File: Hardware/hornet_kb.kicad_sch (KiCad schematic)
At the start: 34 parts, among them J1 Conn_ST_STDC14, J10 USB_C_Receptacle_USB2.0, SW98 SW_Push, U1 nRF52840, Y1 32.768kHz, Y3 Crystal_GND24

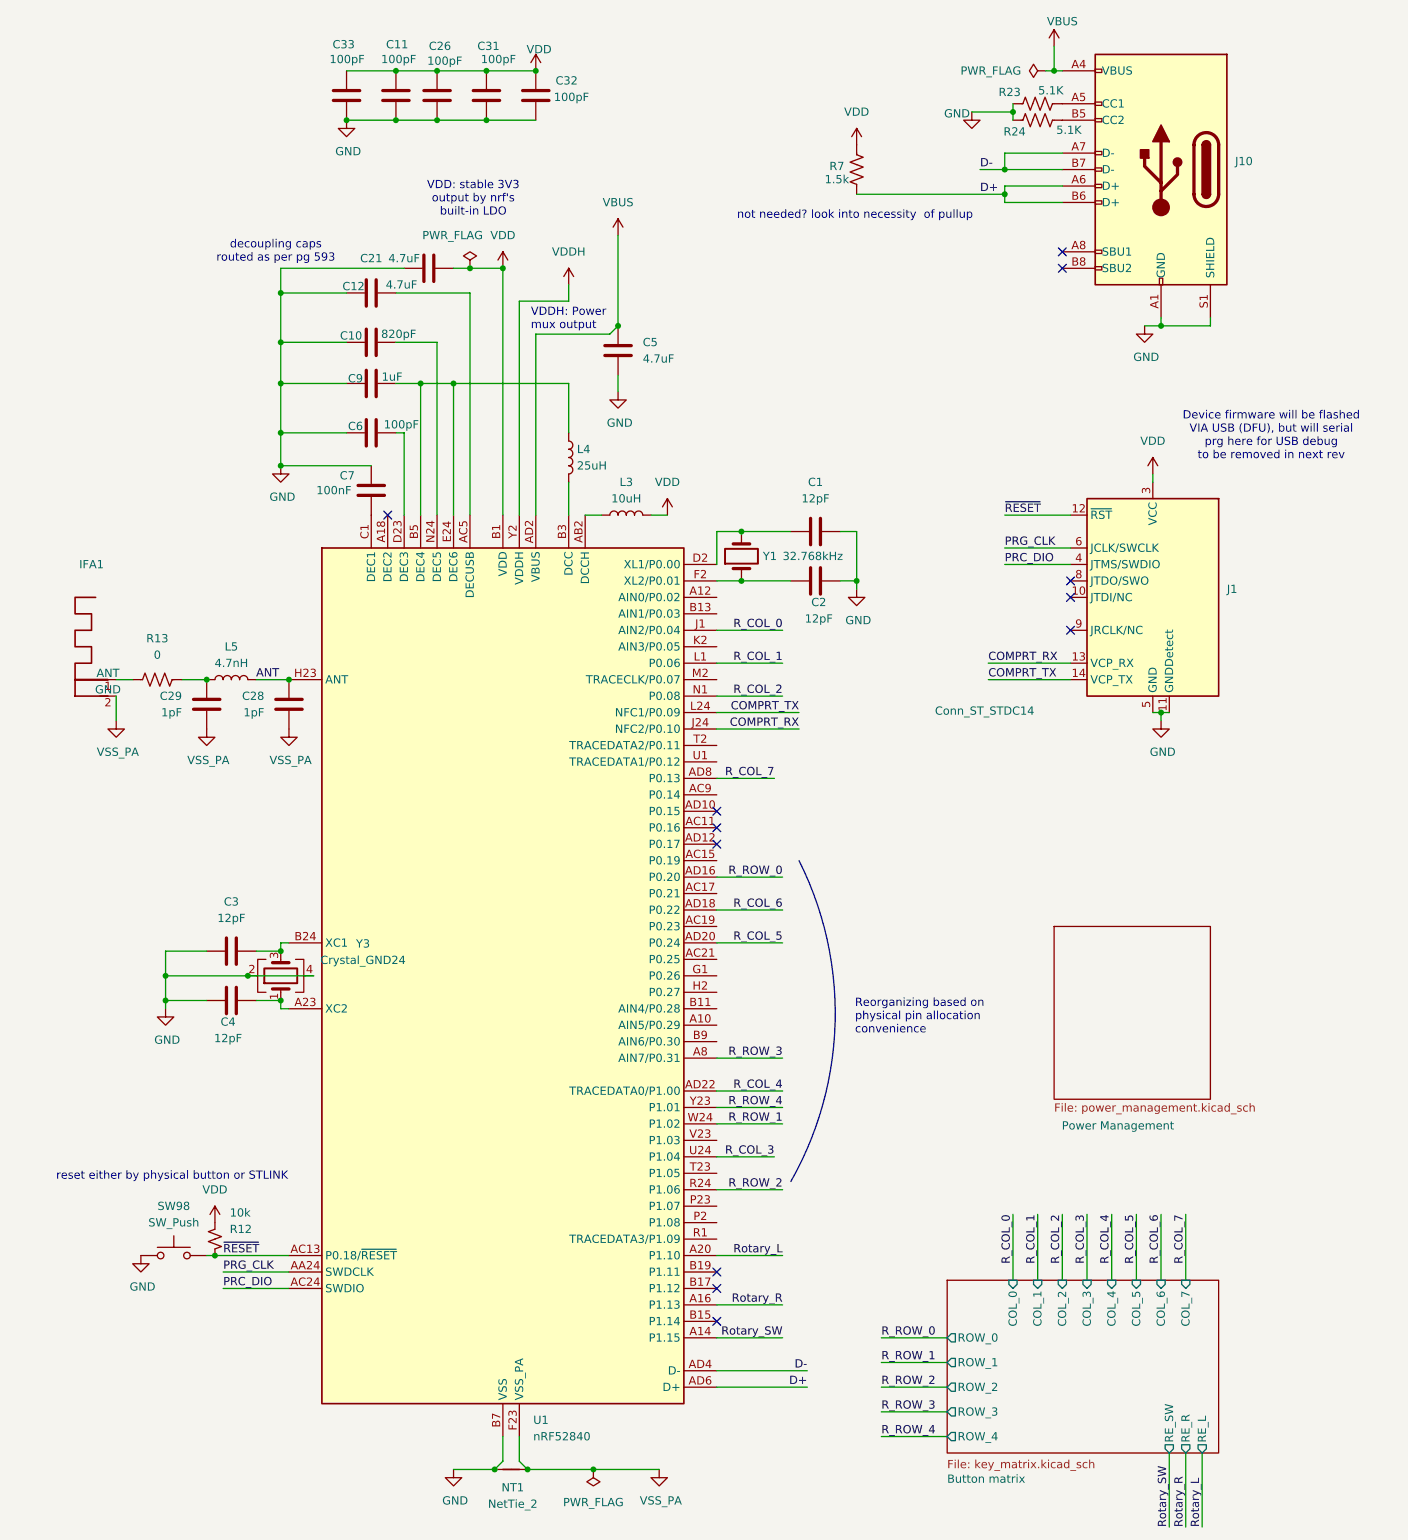
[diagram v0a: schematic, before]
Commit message: Resolving DRC errors
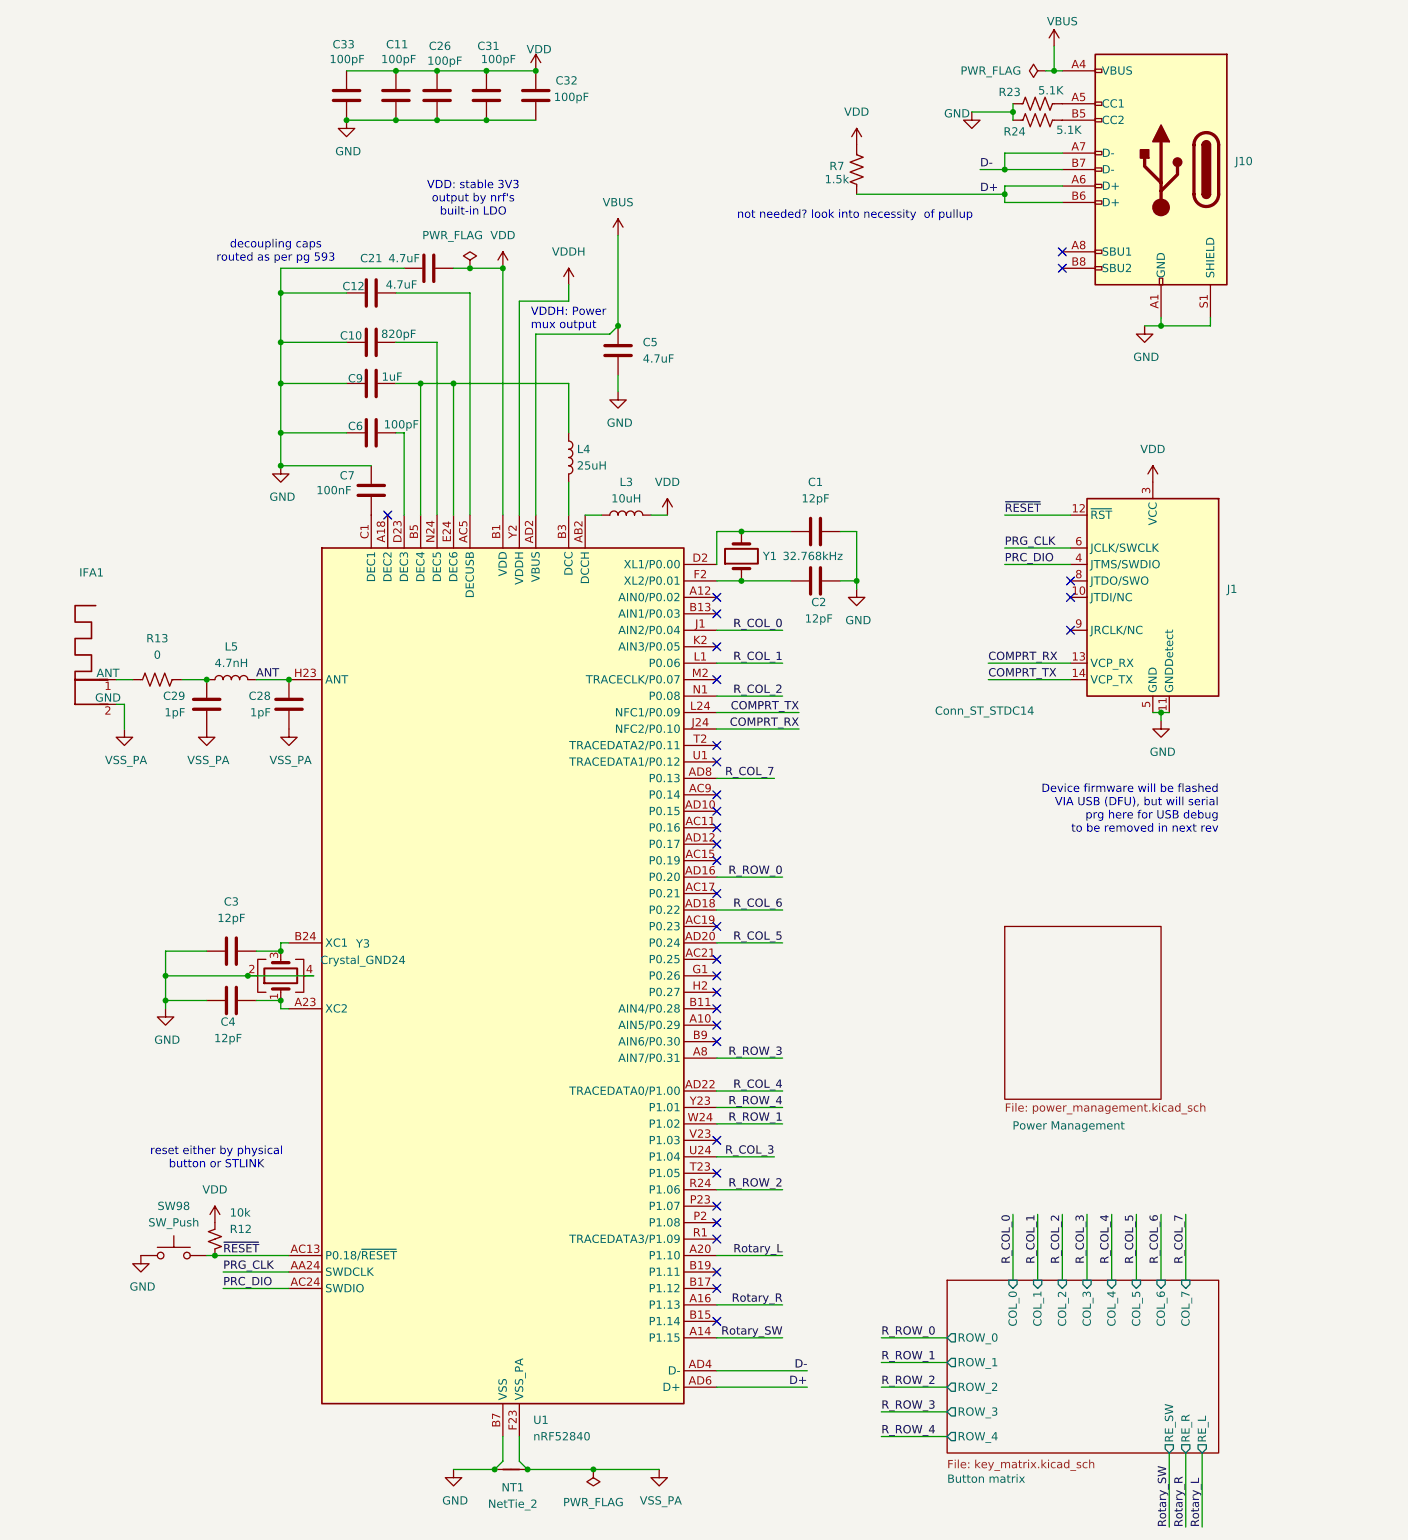
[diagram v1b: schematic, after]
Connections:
- no-connect marks 12 -> 33
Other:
- note removed: "Reorganizing based on physical pin allocation convenience"
- moved on the sheet: IFA1

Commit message: Change reset switchto custom footprint
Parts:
- SW98: footprint Button_Switch_SMD:SW_Push_1P1T-MP_NO_Horizontal_Alps_SKRTLAE010 -> ScottoKeebs_Miscellaneous:SW_DIP_SPSTx01_Slide_6.7x4.1mm_W6.73mm_P2.54mm_LowProfile_JPin
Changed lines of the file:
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@@
 			)
 		)
-		(property "Footprint" "Button_Switch_SMD:SW_Push_1P1T-MP_NO_Horizontal_Alps_SKRTLAE010"
+		(property "Footprint" "ScottoKeebs_Miscellaneous:SW_DIP_SPSTx01_Slide_6.7x4.1mm_W6.73mm_P2.54mm_LowProfile_JPin"
 			(at 29.21 200.66 0)
 			(effects

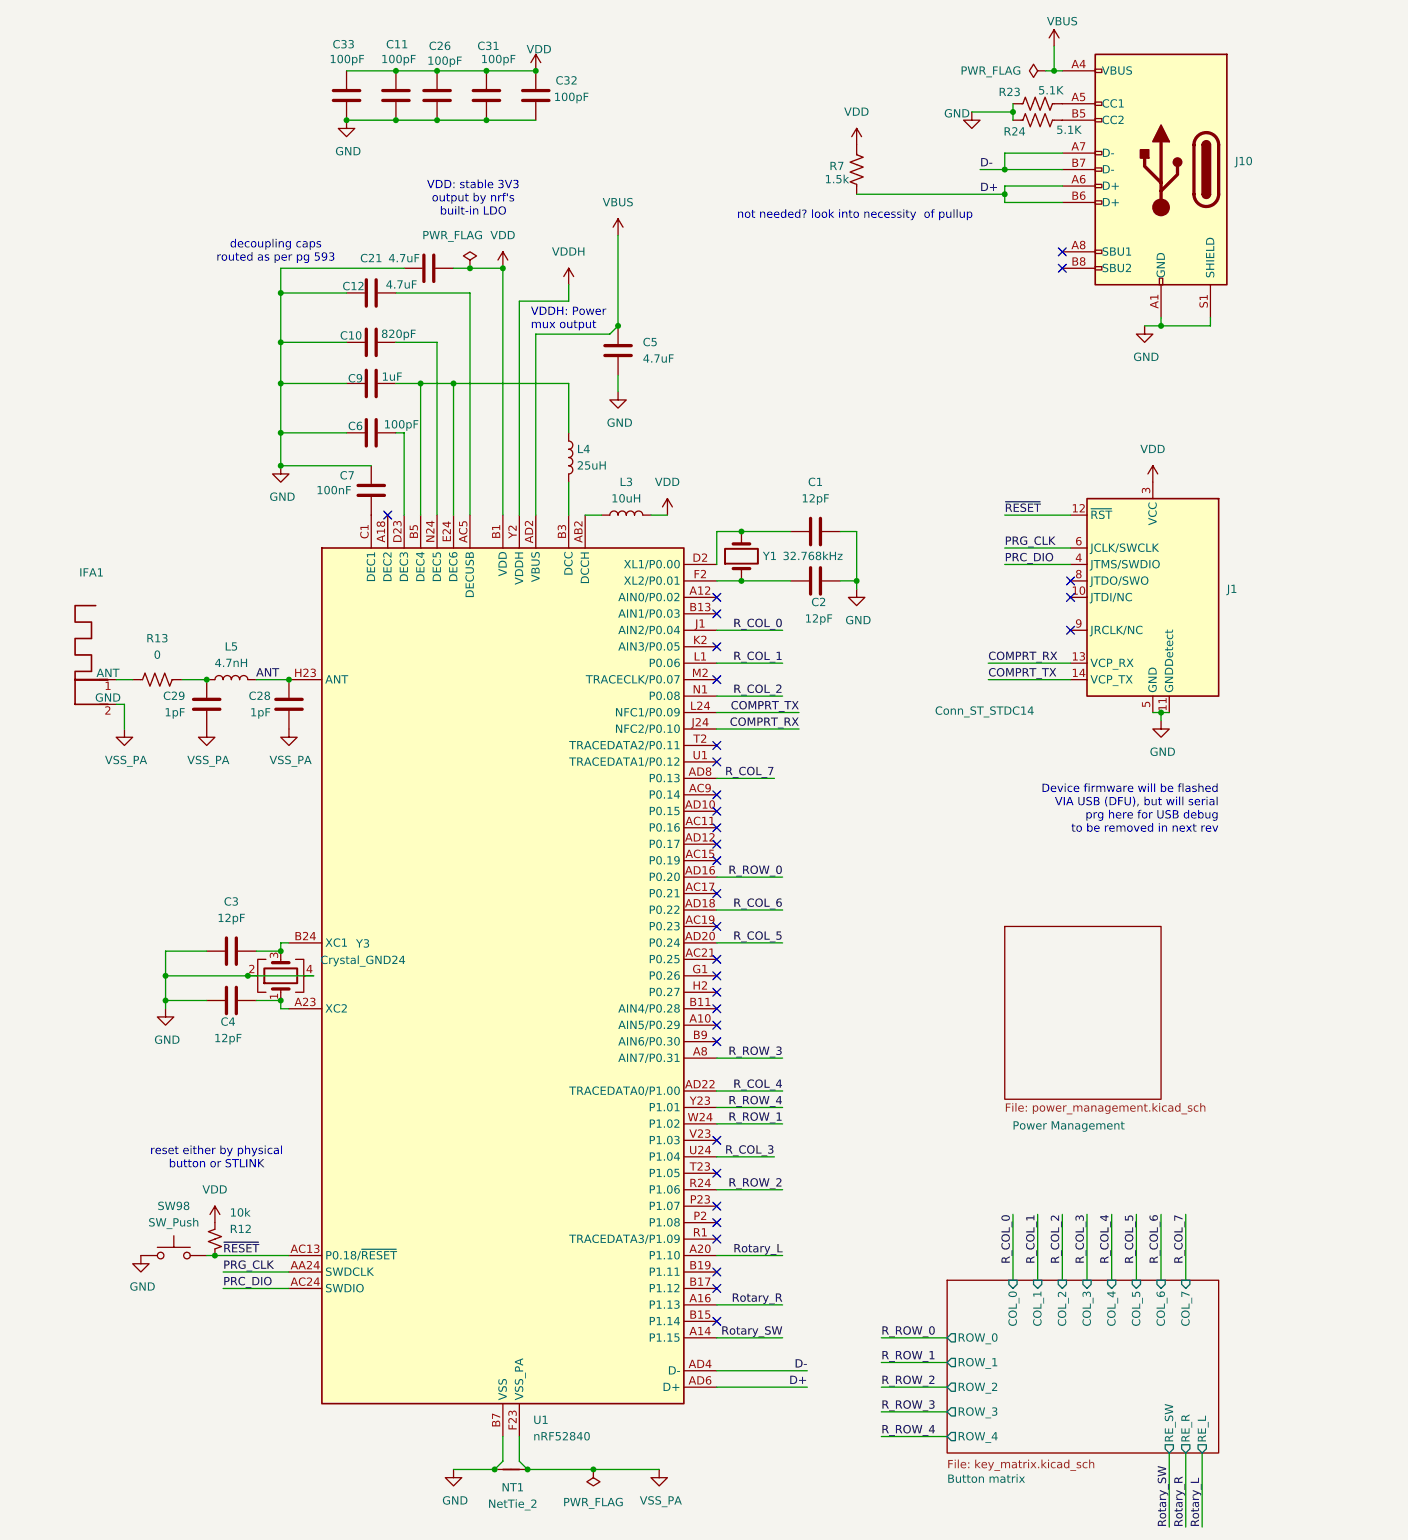
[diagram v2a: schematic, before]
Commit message: added mounting holes
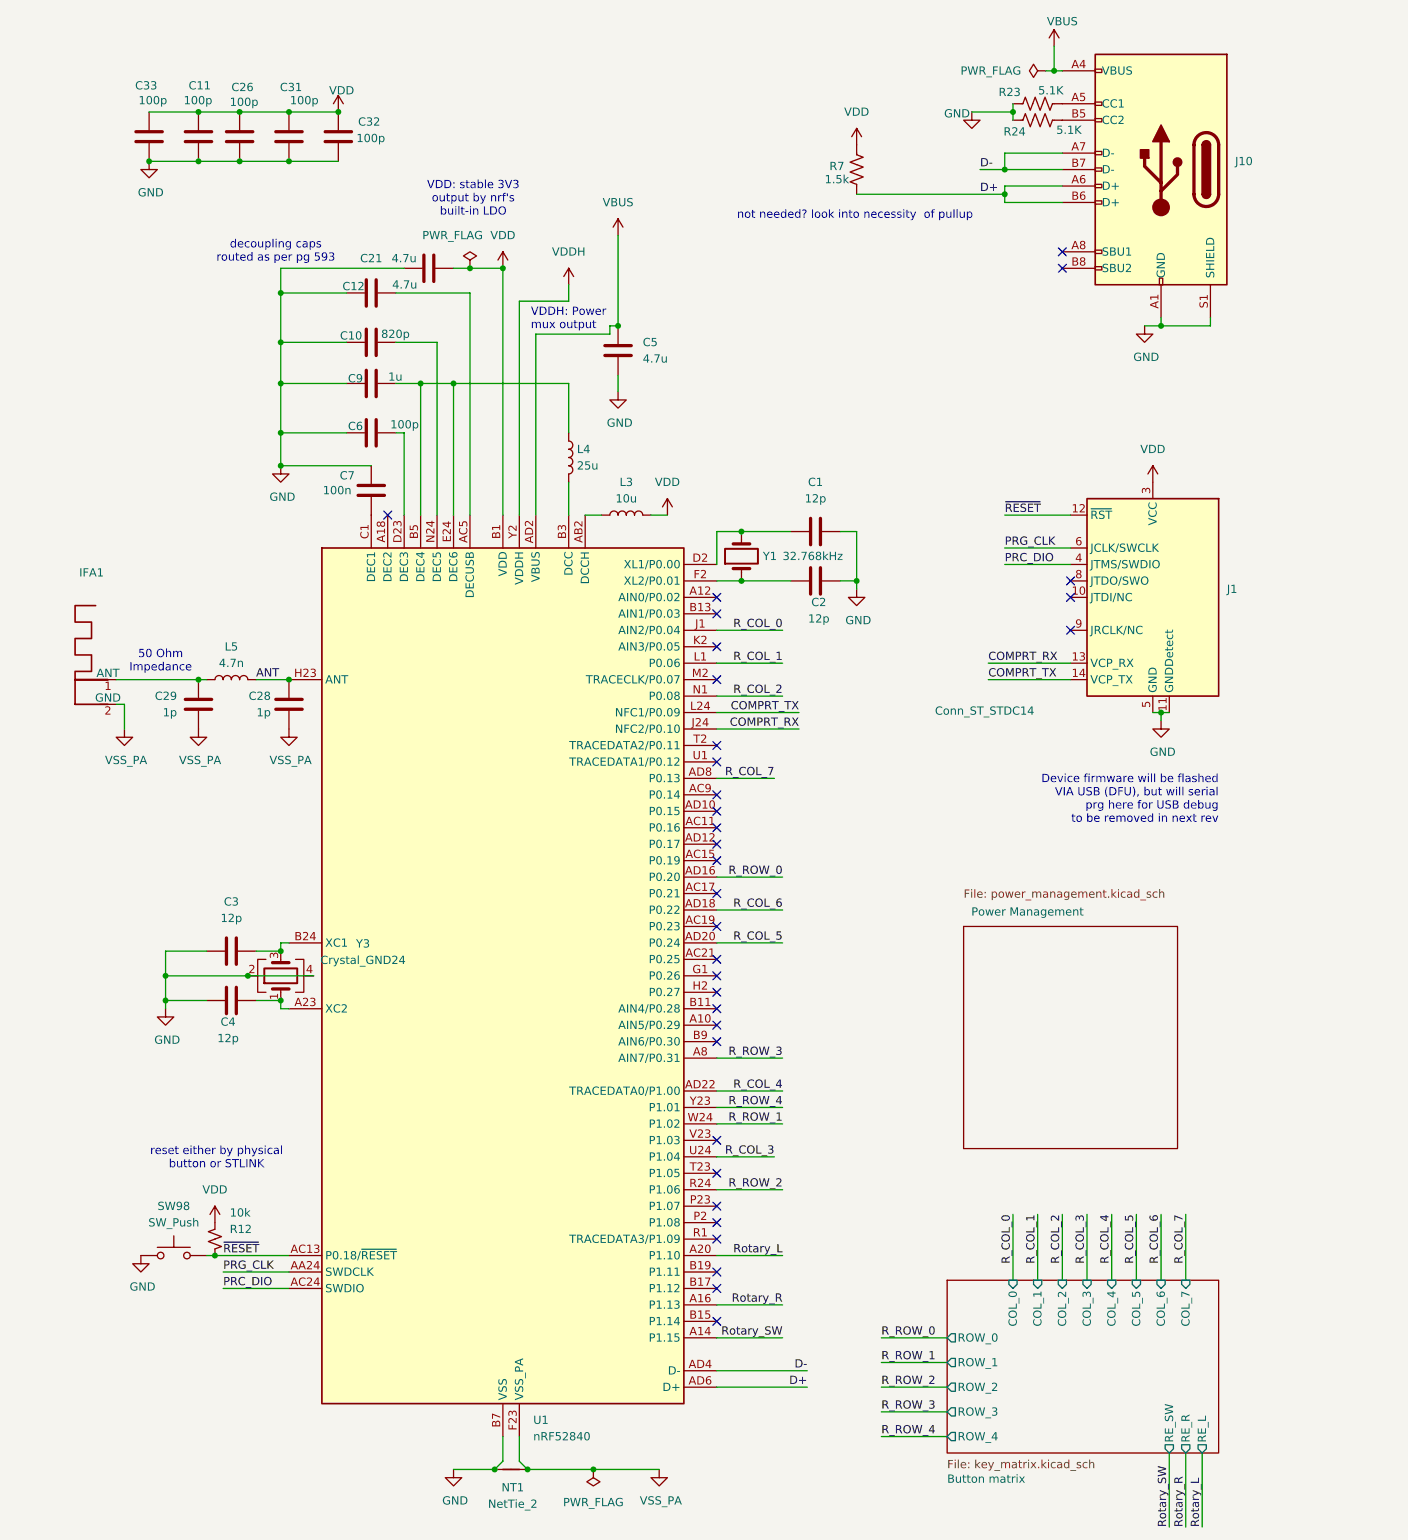
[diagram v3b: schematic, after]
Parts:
- removed R13: 0, Resistor_SMD:R_0402_1005Metric, symbol Device:R_US
- C1, C2, C3, C4: value 12pF -> 12p
- C10: value 820pF -> 820p
- C11, C26, C31, C32, C33, C6: value 100pF -> 100p
- C12, C21, C5: value 4.7uF -> 4.7u
- C28, C29: value 1pF -> 1p
- C7: value 100nF -> 100n
- C9: value 1uF -> 1u
- IFA1: now left out of the parts list
- L3: value 10uH -> 10u
- L4: value 25uH -> 25u
- L5: value 4.7nH -> 4.7n
- SW98: LCSC (none) -> C720477
- U1: LCSC (none) -> C190794
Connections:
- net at IFA1.1 (ANT): now also C29.1, L5.2
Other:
- note added: "50 Ohm Impedance"
- moved on the sheet: C11, C26, C29, C31, C32, C33
